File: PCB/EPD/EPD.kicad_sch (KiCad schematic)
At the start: 68 parts, among them J1 Conn_01x26, J2 Shelly, J3 USB-PROG, J4 BTN1, J6 BTN2, J7 USB-C-Socket-V, J8 PWR, P1 +, P10 2, P11 1, P12 1, P2 -, P3 2, P4 2, P5 1, P6 1, P7 +, P8 -, P9 2, Q1 DMG1012T, U2 ESP32-S3-MINI-1, U3 MD8942

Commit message: Updated
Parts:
- removed C3 (x9): 1uF 50V, RevK:C_0402, symbol Device:C
- removed C3: 100nF 50V, RevK:C_0402, symbol Device:C
- removed C3: 4.7uF, RevK:C_0402, symbol Device:C
- removed C3: 10uF, RevK:C_0402, symbol Device:C
- removed R1: 10K, RevK:R_0402, symbol Device:R
- removed R1: 0.47R, RevK:R_0402, symbol Device:R
- removed R1: 3R, RevK:R_0402, symbol Device:R
- added C3 (x7): 1uF 25V, RevK:C_0402, symbol Device:C
- added C3 (x2): 1uF 10V, RevK:C_0402, symbol Device:C
- added C3: 1uF 50V, RevK:C_0402, symbol Device:C
- added C3 (x2): 4.7uF, RevK:C_0402, symbol Device:C
- added R1: 0.47R, RevK:R_0402, symbol Device:R
- added R1: 10K, RevK:R_0402, symbol Device:R
- added R1: 3R, RevK:R_0402, symbol Device:R
- D1, D2, D3: value 1N5819W -> MBR0530; LCSC Part # C2905650 -> C5204746
- L1: value 68uH -> 10uH; footprint RevK:L_0805 -> RevK:L_4x4; LCSC Part # C275376 -> C38117
- Q1: value DMG1012T -> BSS138; footprint RevK:SOT-323_SC-70-3 -> RevK:SOT-23; LCSC Part # C469327 -> C5279927
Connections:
- net +3.3V: now also JP2.3 (B), C3.1, C3.2; no longer JP1.3 (B)
- net GND: now also D1.1 (K), JP2.1 (A), C3.1, C3.2, C3.2, C3.2, C3.2, C3.2, C3.2, C3.2, C3.2, C3.2, C3.2, R1.1, R1.1, R1.2; no longer D3.1 (K), JP1.1 (A)
- net at J1.2 (Pin_2), Q1.1 (G): now also R1.2
- net at J1.3 (Pin_3), Q1.2 (S): now also JP1.2 (C); no longer JP2.2 (C)
- net at L1.1, Q1.3 (D): now also D3.2 (A), C3.1; no longer D2.2 (A)
- net at D1.2 (A): now also D2.1 (K), C3.2; no longer J1.23 (Pin_23)
- net at J1.5 (Pin_5): now also C3.1
- net at J1.21 (Pin_21): now also D3.1 (K), C3.1; no longer D2.1 (K)
- net at J1.22 (Pin_22): now also C3.1
- net at J1.18 (Pin_18): now also C3.1
- net at J1.19 (Pin_19): now also C3.1
- net at J1.20 (Pin_20): now also C3.1
- net at J1.24 (Pin_24): now also C3.1
- net at J1.4 (Pin_4): now also C3.1
- net at J1.8 (Pin_8): now also JP2.2 (C); no longer JP1.2 (C)
- new net: JP1.1 (A), R1.1
- new net: C3.1, D2.2 (A), J1.23 (Pin_23)
- new net: JP1.3 (B), R1.2

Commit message: For order
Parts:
- removed Q1: BSS138, RevK:SOT-23, symbol RevK:Si1308EDL
- added Q1: BSS138, RevK:SOT-23, symbol Transistor_FET:BSS138
- D4: JLCPCB Rotation Offset -90 -> 0; LCSC Part # (none) -> C96225
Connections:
- net at C3.1, D3.2 (A), L1.1: now also Q1.3 (D)
- net at J1.2 (Pin_2), R1.2: now also Q1.1 (G)
- net at J1.3 (Pin_3), JP1.2 (C): now also Q1.2 (S)
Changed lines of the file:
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@@
   (junction (at 255.27 147.955) (diameter 0) (color 0 0 0 0)
   )
+  (junction (at 161.29 102.235) (diameter 0) (color 0 0 0 0)
+  )
+  (junction (at 253.365 147.955) (diameter 0) (color 0 0 0 0)
+  )
+  (junction (at 161.29 107.315) (diameter 0) (color 0 0 0 0)
+  )
   (junction (at 172.085 140.97) (diameter 0) (color 0 0 0 0)
-  )
-  (junction (at 161.29 102.235) (diameter 0) (color 0 0 0 0)
-  )
-  (junction (at 253.365 147.955) (diameter 0) (color 0 0 0 0)
-  )
-  (junction (at 161.29 107.315) (diameter 0) (color 0 0 0 0)
   )
   (junction (at 126.365 112.395) (diameter 0) (color 0 0 0 0)
@@
     (stroke (width 0) (type default))
   )
+  (wire (pts (xy 172.085 140.97) (xy 172.085 156.845))
+    (stroke (width 0) (type default))
+  )
   (wire (pts (xy 248.92 27.305) (xy 250.825 27.305))
     (stroke (width 0) (type default))
@@
     (stroke (width 0) (type default))
   )
-  (wire (pts (xy 172.085 140.97) (xy 172.085 137.16))
-    (stroke (width 0) (type default))
-  )
-  (wire (pts (xy 172.085 140.97) (xy 172.085 156.845))
+  (wire (pts (xy 172.085 137.16) (xy 172.085 140.97))
     (stroke (width 0) (type default))
   )
@@
     )
   )
+  (symbol (lib_id "Transistor_FET:BSS138") (at 177.165 140.97 0) (unit 1)
+    (in_bom yes) (on_board yes) (dnp no) (fields_autoplaced)
+    (property "Reference" "Q1" (at 182.372 139.7579 0)
+      (effects (font (size 1.27 1.27)) (justify left))
+    )
+    (property "Value" "BSS138" (at 182.372 142.1821 0)
+      (effects (font (size 1.27 1.27)) (justify left))
+    )
+    (property "Footprint" "RevK:SOT-23" (at 182.245 142.875 0)
+      (effects (font (size 1.27 1.27) italic) (justify left) hide)
+    )
+    (property "Datasheet" "" (at 177.165 140.97 0)
+      (effects (font (size 1.27 1.27)) (justify left) hide)
+    )
+    (property "LCSC Part #" "C2938375" (at 177.165 140.97 0)
+      (effects (font (size 1.27 1.27)) hide)
+    )
+    (property "JLCPCB Rotation Offset" "180" (at 177.165 140.97 0)
+      (effects (font (size 1.27 1.27)) hide)
+    )
+    (pin "1")
+    (pin "2")
+    (pin "3")
+    (instances
+      (project "EPD"
+        (path "/46c350bb-7de4-4e81-aafd-4af55e37aab0"
+          (reference "Q1") (unit 1)
+        )
+      )
+    )
+  )
   (symbol (lib_id "power:GND") (at 100.965 25.4 0) (unit 1)
     (in_bom yes) (on_board yes) (dnp no) (fields_autoplaced)
@@
       (effects (font (size 1.27 1.27)) hide)
     )
-    (property "JLCPCB Rotation Offset" "-90" (at 221.615 22.225 0)
+    (property "JLCPCB Rotation Offset" "0" (at 221.615 22.225 0)
+      (effects (font (size 1.27 1.27)) hide)
+    )
+    (property "LCSC Part #" "C96225" (at 221.615 22.225 0)
       (effects (font (size 1.27 1.27)) hide)
     )
@@
     )
   )
-  (symbol (lib_id "RevK:Si1308EDL") (at 177.165 140.97 0) (unit 1)
-    (in_bom yes) (on_board yes) (dnp no) (fields_autoplaced)
-    (property "Reference" "Q1" (at 182.372 140.4564 0)
-      (effects (font (size 1.27 1.27)) (justify left))
-    )
-    (property "Value" "BSS138" (at 182.372 142.8806 0)
-      (effects (font (size 1.27 1.27)) (justify left))
-    )
-    (property "Footprint" "RevK:SOT-23" (at 182.245 142.875 0)
-      (effects (font (size 1.27 1.27)) (justify left) hide)
-    )
-    (property "Datasheet" "" (at 177.165 140.97 0)
-      (effects (font (size 1.27 1.27)) hide)
-    )
-    (property "LCSC Part #" "C5279927" (at 177.165 140.97 0)
-      (effects (font (size 1.27 1.27)) hide)
-    )
-    (pin "1")
-    (pin "2")
-    (pin "3")
-    (instances
-      (project "EPD"
-        (path "/46c350bb-7de4-4e81-aafd-4af55e37aab0"
-          (reference "Q1") (unit 1)
-        )
-      )
-    )
-  )
   (symbol (lib_id "Diode:BAV99S") (at 221.615 37.465 0) (unit 2)
     (in_bom yes) (on_board yes) (dnp no)
@@
       (effects (font (size 1.27 1.27)) hide)
     )
-    (property "JLCPCB Rotation Offset" "-90" (at 221.615 37.465 0)
-      (effects (font (size 1.27 1.27)) hide)
-    )
+    (property "JLCPCB Rotation Offset" "0" (at 221.615 37.465 0)
+      (effects (font (size 1.27 1.27)) hide)
+    )
+    (property "LCSC Part #" "C96225" (at 221.615 37.465 0)
+      (effects (font (size 1.27 1.27)) hide)
+    )

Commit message: Tidy
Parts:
- removed D8: D, RevK:D_SOD-123, symbol Device:D
- added D6: MBR0530, RevK:D_SOD-123, symbol Diode:1N5819
- C3: value 1uF 10V -> 1uF
- C3: footprint RevK:C_0402 -> RevK:C_0603
- L1: LCSC Part # C38117 -> (none)
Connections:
- net PWR: now also D6.1 (K)
- net at J7.A4 (VBUS), J7.A9 (VBUS), J7.B4 (VBUS)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: now also D6.2 (A)
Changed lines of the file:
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@@
       (effects (font (size 1.27 1.27)))
     )
-    (property "Value" "1uF 10V" (at 139.7 106.045 90)
+    (property "Value" "1uF" (at 139.7 106.045 90)
       (effects (font (size 1.27 1.27)))
     )
@@
       (effects (font (size 1.27 1.27)))
     )
-    (property "Footprint" "RevK:C_0402" (at 149.86 88.5698 0)
+    (property "Footprint" "RevK:C_0603" (at 149.86 88.5698 0)
       (effects (font (size 1.27 1.27)) hide)
     )
@@
         (path "/46c350bb-7de4-4e81-aafd-4af55e37aab0"
           (reference "#PWR013") (unit 1)
-        )
-      )
-    )
-  )
-  (symbol (lib_id "Device:D") (at 266.7 84.455 180) (unit 1)
-    (in_bom yes) (on_board yes) (dnp no)
-    (property "Reference" "D8" (at 266.7 78.9432 0)
-      (effects (font (size 1.27 1.27)))
-    )
-    (property "Value" "D" (at 266.7 81.2546 0)
-      (effects (font (size 1.27 1.27)))
-    )
-    (property "Footprint" "RevK:D_SOD-123" (at 266.7 84.455 0)
-      (effects (font (size 1.27 1.27)) hide)
-    )
-    (property "Datasheet" "~" (at 266.7 84.455 0)
-      (effects (font (size 1.27 1.27)) hide)
-    )
-    (property "LCSC Part #" "C1884542" (at 266.7 84.455 0)
-      (effects (font (size 1.27 1.27)) hide)
-    )
-    (property "Sim.Device" "D" (at 266.7 84.455 0)
-      (effects (font (size 1.27 1.27)) hide)
-    )
-    (property "Sim.Pins" "1=K 2=A" (at 266.7 84.455 0)
-      (effects (font (size 1.27 1.27)) hide)
-    )
-    (pin "1")
-    (pin "2")
-    (instances
-      (project "Access"
-        (path "/2a267270-6585-45e3-a633-b53049f10066"
-          (reference "D8") (unit 1)
-        )
-      )
-      (project "GenericS3"
-        (path "/2d210a96-f81f-42a9-8bf4-1b43c11086f3"
-          (reference "D1") (unit 1)
-        )
-      )
-      (project "EPD"
-        (path "/46c350bb-7de4-4e81-aafd-4af55e37aab0"
-          (reference "D6") (unit 1)
         )
       )
@@
       (effects (font (size 1.27 1.27)) hide)
     )
-    (property "Part No" "" (at 185.42 45.72 0)
-      (effects (font (size 1.27 1.27)) hide)
-    )
-    (property "Note" "" (at 185.42 45.72 0)
-      (effects (font (size 1.27 1.27)) hide)
-    )
     (instances
       (project "EPD"
@@
       (effects (font (size 1.27 1.27)))
     )
-    (property "Value" "1uF 10V" (at 139.7 111.125 90)
+    (property "Value" "1uF" (at 139.7 111.125 90)
       (effects (font (size 1.27 1.27)))
     )
@@
   (symbol (lib_id "Device:C") (at 87.63 106.045 0) (unit 1)
     (in_bom yes) (on_board yes) (dnp no) (fields_autoplaced)
-    (property "Reference" "C3" (at 90.551 105.2103 0)
-      (effects (font (size 1.27 1.27)) (justify left))
-    )
-    (property "Value" "1uF" (at 90.551 107.7472 0)
+    (property "Reference" "C3" (at 90.551 104.8329 0)
+      (effects (font (size 1.27 1.27)) (justify left))
+    )
+    (property "Value" "1uF" (at 90.551 107.2571 0)
       (effects (font (size 1.27 1.27)) (justify left))
     )
@@
     )
   )
+  (symbol (lib_id "Diode:1N5819") (at 266.7 84.455 180) (unit 1)
+    (in_bom yes) (on_board yes) (dnp no)
+    (property "Reference" "D6" (at 263.525 83.185 0)
+      (effects (font (size 1.27 1.27)))
+    )
+    (property "Value" "MBR0530" (at 266.065 80.645 0)
+      (effects (font (size 1.27 1.27)))
+    )
+    (property "Footprint" "RevK:D_SOD-123" (at 266.7 80.01 0)
+      (effects (font (size 1.27 1.27)) hide)
+    )
+    (property "Datasheet" "" (at 266.7 84.455 0)
+      (effects (font (size 1.27 1.27)) hide)
+    )
+    (property "LCSC Part #" "C5204746" (at 266.7 84.455 0)
+      (effects (font (size 1.27 1.27)) hide)
+    )
+    (pin "1")
+    (pin "2")
+    (instances
+      (project "EPD"
+        (path "/46c350bb-7de4-4e81-aafd-4af55e37aab0"
+          (reference "D6") (unit 1)
+        )
+      )
+    )
+  )
   (symbol (lib_id "RevK:VCUT") (at 274.32 170.815 0) (unit 1)
     (in_bom no) (on_board yes) (dnp no) (fields_autoplaced)
@@
       (effects (font (size 1.27 1.27)) hide)
     )
-    (property "LCSC Part #" "C38117" (at 187.96 93.98 0)
-      (effects (font (size 1.27 1.27)) hide)
-    )

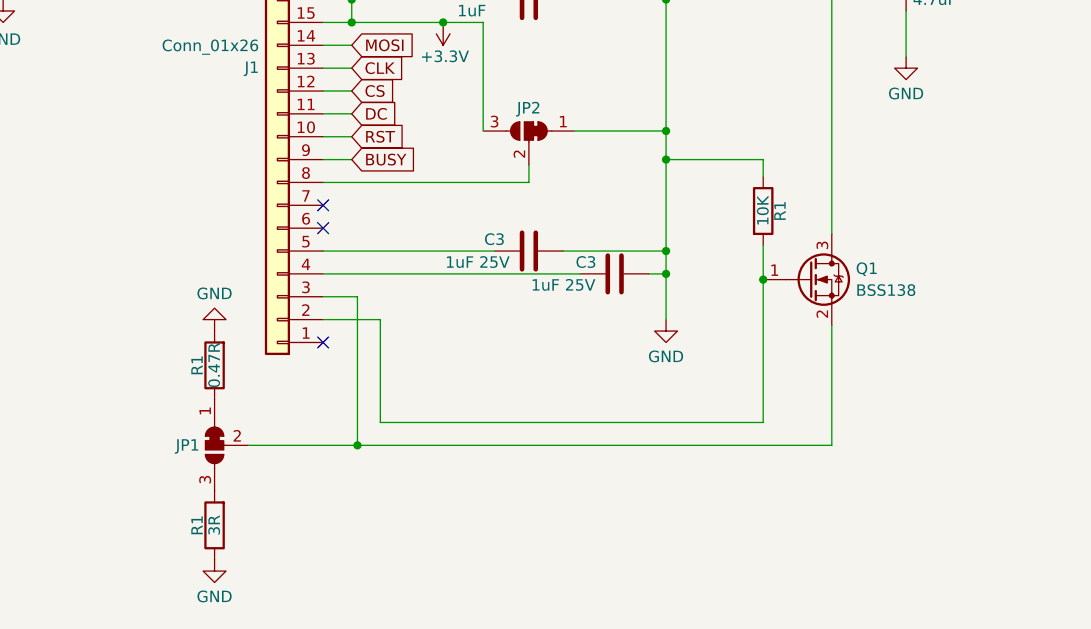
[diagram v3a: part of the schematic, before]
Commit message: Updated so RESE is cleaner
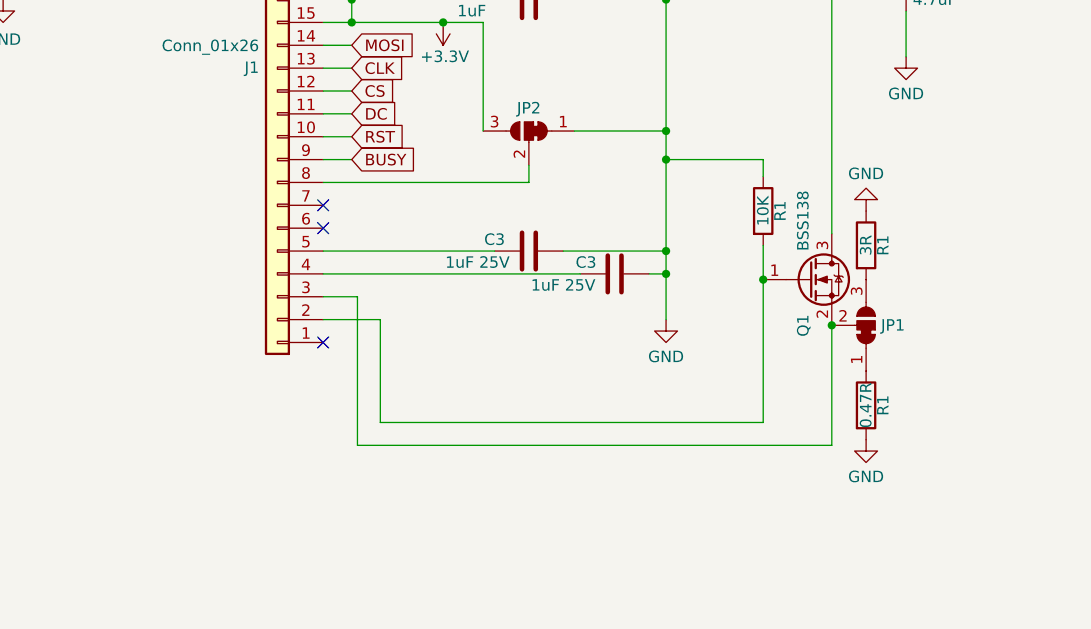
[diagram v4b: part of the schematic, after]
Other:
- moved on the sheet: JP1, R1
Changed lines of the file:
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@@
   (junction (at 161.29 137.795) (diameter 0) (color 0 0 0 0)
   )
-  (junction (at 127 159.385) (diameter 0) (color 0 0 0 0)
-  )
   (junction (at 161.29 109.855) (diameter 0) (color 0 0 0 0)
   )
@@
   (junction (at 131.445 92.075) (diameter 0) (color 0 0 0 0)
   )
+  (junction (at 179.705 146.05) (diameter 0) (color 0 0 0 0)
+  )
   (junction (at 187.96 77.47) (diameter 0) (color 0 0 0 0)
   )
@@
     (stroke (width 0) (type default))
   )
-  (wire (pts (xy 114.935 159.385) (xy 127 159.385))
-    (stroke (width 0) (type default))
-  )
   (wire (pts (xy 255.27 147.955) (xy 256.54 147.955))
     (stroke (width 0) (type default))
@@
   )
   (symbol (lib_id "Transistor_FET:BSS138") (at 177.165 140.97 0) (unit 1)
-    (in_bom yes) (on_board yes) (dnp no) (fields_autoplaced)
-    (property "Reference" "Q1" (at 182.372 139.7579 0)
+    (in_bom yes) (on_board yes) (dnp no)
+    (property "Reference" "Q1" (at 176.53 147.32 90)
       (effects (font (size 1.27 1.27)) (justify left))
     )
-    (property "Value" "BSS138" (at 182.372 142.1821 0)
+    (property "Value" "BSS138" (at 176.53 137.795 90)
       (effects (font (size 1.27 1.27)) (justify left))
     )
@@
     )
   )
-  (symbol (lib_id "Device:R") (at 111.125 150.495 180) (unit 1)
+  (symbol (lib_id "Device:R") (at 183.515 154.94 0) (unit 1)
     (in_bom yes) (on_board yes) (dnp no)
-    (property "Reference" "R1" (at 109.22 150.495 90)
+    (property "Reference" "R1" (at 185.42 154.94 90)
       (effects (font (size 1.27 1.27)))
     )
-    (property "Value" "0.47R" (at 111.125 150.495 90)
+    (property "Value" "0.47R" (at 183.515 154.94 90)
       (effects (font (size 1.27 1.27)))
     )
-    (property "Footprint" "RevK:R_0402" (at 112.903 150.495 90)
+    (property "Footprint" "RevK:R_0402" (at 181.737 154.94 90)
       (effects (font (size 1.27 1.27)) hide)
     )
-    (property "Datasheet" "~" (at 111.125 150.495 0)
+    (property "Datasheet" "~" (at 183.515 154.94 0)
       (effects (font (size 1.27 1.27)) hide)
     )
@@
     )
   )
-  (symbol (lib_id "power:GND") (at 111.125 146.685 180) (unit 1)
+  (symbol (lib_id "power:GND") (at 183.515 158.75 0) (unit 1)
     (in_bom yes) (on_board yes) (dnp no) (fields_autoplaced)
-    (property "Reference" "#PWR0105" (at 111.125 140.335 0)
+    (property "Reference" "#PWR0105" (at 183.515 165.1 0)
       (effects (font (size 1.27 1.27)) hide)
     )
-    (property "Value" "GND" (at 111.125 142.5519 0)
+    (property "Value" "GND" (at 183.515 162.8831 0)
       (effects (font (size 1.27 1.27)))
     )
-    (property "Footprint" "" (at 111.125 146.685 0)
+    (property "Footprint" "" (at 183.515 158.75 0)
       (effects (font (size 1.27 1.27)) hide)
     )
-    (property "Datasheet" "" (at 111.125 146.685 0)
+    (property "Datasheet" "" (at 183.515 158.75 0)
       (effects (font (size 1.27 1.27)) hide)
     )
@@
     )
   )
-  (symbol (lib_id "Device:R") (at 111.125 168.275 180) (unit 1)
+  (symbol (lib_id "Device:R") (at 183.515 137.16 0) (unit 1)
     (in_bom yes) (on_board yes) (dnp no)
-    (property "Reference" "R1" (at 109.22 168.275 90)
+    (property "Reference" "R1" (at 185.42 137.16 90)
       (effects (font (size 1.27 1.27)))
     )
-    (property "Value" "3R" (at 111.125 168.275 90)
+    (property "Value" "3R" (at 183.515 137.16 90)
       (effects (font (size 1.27 1.27)))
     )
-    (property "Footprint" "RevK:R_0402" (at 112.903 168.275 90)
+    (property "Footprint" "RevK:R_0402" (at 181.737 137.16 90)
       (effects (font (size 1.27 1.27)) hide)
     )
-    (property "Datasheet" "~" (at 111.125 168.275 0)
+    (property "Datasheet" "~" (at 183.515 137.16 0)
       (effects (font (size 1.27 1.27)) hide)
     )
@@
     )
   )
-  (symbol (lib_id "Jumper:SolderJumper_3_Bridged12") (at 111.125 159.385 90) (mirror x) (unit 1)
+  (symbol (lib_id "Jumper:SolderJumper_3_Bridged12") (at 183.515 146.05 270) (mirror x) (unit 1)
     (in_bom no) (on_board yes) (dnp no)
-    (property "Reference" "JP1" (at 109.4741 159.385 90)
+    (property "Reference" "JP1" (at 185.1659 146.05 90)
       (effects (font (size 1.27 1.27)) (justify left))
     )
-    (property "Value" "SolderJumper_3_Bridged12" (at 108.5159 159.385 0)
+    (property "Value" "SolderJumper_3_Bridged12" (at 186.1241 146.05 0)
       (effects (font (size 1.27 1.27)) hide)
     )
-    (property "Footprint" "RevK:SolderJumper3" (at 111.125 159.385 0)
+    (property "Footprint" "RevK:SolderJumper3" (at 183.515 146.05 0)
       (effects (font (size 1.27 1.27)) hide)
     )
-    (property "Datasheet" "~" (at 111.125 159.385 0)
+    (property "Datasheet" "~" (at 183.515 146.05 0)
       (effects (font (size 1.27 1.27)) hide)
     )
@@
     )
   )
-  (symbol (lib_id "power:GND") (at 111.125 172.085 0) (unit 1)
+  (symbol (lib_id "power:GND") (at 183.515 133.35 180) (unit 1)
     (in_bom yes) (on_board yes) (dnp no) (fields_autoplaced)
-    (property "Reference" "#PWR0105" (at 111.125 178.435 0)
+    (property "Reference" "#PWR0105" (at 183.515 127 0)
       (effects (font (size 1.27 1.27)) hide)
     )
-    (property "Value" "GND" (at 111.125 176.2181 0)
+    (property "Value" "GND" (at 183.515 129.2169 0)
       (effects (font (size 1.27 1.27)))
     )
-    (property "Footprint" "" (at 111.125 172.085 0)
+    (property "Footprint" "" (at 183.515 133.35 0)
       (effects (font (size 1.27 1.27)) hide)
     )
-    (property "Datasheet" "" (at 111.125 172.085 0)
+    (property "Datasheet" "" (at 183.515 133.35 0)
       (effects (font (size 1.27 1.27)) hide)
     )

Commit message: Missing VBUS!
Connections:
- net VBUS: now also D6.2 (A), J7.A4 (VBUS), J7.A9 (VBUS), J7.B4 (VBUS), J7.B9 (VBUS)
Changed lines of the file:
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@@
   (junction (at 161.29 102.235) (diameter 0) (color 0 0 0 0)
   )
+  (junction (at 262.89 84.455) (diameter 0) (color 0 0 0 0)
+  )
   (junction (at 253.365 147.955) (diameter 0) (color 0 0 0 0)
   )
@@
     (stroke (width 0) (type default))
   )
+  (wire (pts (xy 262.89 76.835) (xy 262.89 84.455))
+    (stroke (width 0) (type default))
+  )
   (wire (pts (xy 255.27 145.415) (xy 256.54 145.415))
     (stroke (width 0) (type default))
@@
     )
   )
+  (global_label "VBUS" (shape output) (at 262.89 76.835 90) (fields_autoplaced)
+    (effects (font (size 1.27 1.27)) (justify left))
+    (property "Intersheetrefs" "${INTERSHEET_REFS}" (at 262.89 69.6054 90)
+      (effects (font (size 1.27 1.27)) (justify left) hide)
+    )
+  )
   (global_label "RST" (shape input) (at 126.365 125.095 0) (fields_autoplaced)
     (effects (font (size 1.27 1.27)) (justify left))
@@
   (symbol (lib_id "Diode:1N5819") (at 266.7 84.455 180) (unit 1)
     (in_bom yes) (on_board yes) (dnp no)
-    (property "Reference" "D6" (at 263.525 83.185 0)
+    (property "Reference" "D6" (at 267.97 81.915 0)
       (effects (font (size 1.27 1.27)))
     )
-    (property "Value" "MBR0530" (at 266.065 80.645 0)
+    (property "Value" "MBR0530" (at 271.145 80.01 0)
       (effects (font (size 1.27 1.27)))
     )

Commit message: Smaller
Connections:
- net GND: now also U2.9 (GPIO5)
- no-connect marks 28 -> 27
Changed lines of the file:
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@@
   (no_connect (at 79.375 99.06))
   (no_connect (at 79.375 96.52))
-  (no_connect (at 48.895 58.42))
   (no_connect (at 153.035 45.72))
   (no_connect (at 48.895 53.34))
@@
         )
       )
+    )
+  )
+  (symbol (lib_id "power:GND") (at 48.895 58.42 270) (unit 1)
+    (in_bom yes) (on_board yes) (dnp no) (fields_autoplaced)
+    (property "Reference" "#PWR01" (at 42.545 58.42 0)
+      (effects (font (size 1.27 1.27)) hide)
+    )
+    (property "Value" "GND" (at 45.7201 58.42 90)
+      (effects (font (size 1.27 1.27)) (justify right))
+    )
+    (property "Footprint" "" (at 48.895 58.42 0)
+      (effects (font (size 1.27 1.27)) hide)
+    )
+    (property "Datasheet" "" (at 48.895 58.42 0)
+      (effects (font (size 1.27 1.27)) hide)
+    )
+    (pin "1")
+    (instances
+      (project "USBA"
+        (path "/2d210a96-f81f-42a9-8bf4-1b43c11086f3"
+          (reference "#PWR01") (unit 1)
+        )
+      )
+      (project "EPD"
+        (path "/46c350bb-7de4-4e81-aafd-4af55e37aab0"
+          (reference "#PWR021") (unit 1)
+        )
+      )
